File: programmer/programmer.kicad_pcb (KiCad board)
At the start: 2 copper layers, 63 x 30 mm, 54 parts, among them J1 USB_C_Receptacle_USB2.0_14P, U1 FT2232HL, U2 74LVC2T45DC, U3 93CxxA, U4 NLSV2T244DM, U5 NLSV2T244DM, U6 NLSV2T244DM, U8 AMS1117-3.3, Y1 12MHz

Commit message: Programmer bring-up changes and notes
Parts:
- added C20: 3.3u, Capacitor_SMD:C_0603_1608Metric_Pad1.08x0.95mm_HandSolder, F.Cu at (59.6, 35.5)
- added C21: 3.3u, Capacitor_SMD:C_0603_1608Metric_Pad1.08x0.95mm_HandSolder, F.Cu at (59.9, 30.4)
- added C22: 3.3u, Capacitor_SMD:C_0603_1608Metric_Pad1.08x0.95mm_HandSolder, F.Cu at (59.8, 25.3)
- added R12: 2.2, Resistor_SMD:R_0603_1608Metric_Pad0.98x0.95mm_HandSolder, F.Cu at (83.6, 22.4)
- added TP1: TestPoint, TestPoint:TestPoint_THTPad_1.0x1.0mm_Drill0.5mm, F.Cu at (72.5, 23.6)
- added TP2: TestPoint, TestPoint:TestPoint_THTPad_1.0x1.0mm_Drill0.5mm, F.Cu at (70.4, 23.6)
- added TP3: TestPoint, TestPoint:TestPoint_THTPad_1.0x1.0mm_Drill0.5mm, F.Cu at (70.4, 25.7)
- added TP4: TestPoint, TestPoint:TestPoint_THTPad_1.0x1.0mm_Drill0.5mm, F.Cu at (69.6, 37.0)
- added TP5: TestPoint, TestPoint:TestPoint_THTPad_1.0x1.0mm_Drill0.5mm, F.Cu at (69.6, 34.9)
- added TP6: TestPoint, TestPoint:TestPoint_THTPad_1.0x1.0mm_Drill0.5mm, F.Cu at (69.6, 32.8)
- C6: value 3.3u -> 22u; footprint Capacitor_SMD:C_0603_1608Metric_Pad1.08x0.95mm_HandSolder -> Capacitor_SMD:C_0805_2012Metric_Pad1.18x1.45mm_HandSolder
- moved C7 0.70 mm to (85.9, 26.9), turned to -90 degrees
- moved C6 0.12 mm to (85.5, 22.6), turned to 90 degrees
- turned D4 to 90 degrees
- turned D5 to 90 degrees
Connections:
- C6 pad 2: GND -> Net-(C6-Pad2)
- D4 pad 1: VCC -> Net-(D4-K)
- D4 pad 2: Net-(D4-A) -> VCC
- D5 pad 1: VIO -> Net-(D5-K)
- D5 pad 2: Net-(D5-A) -> VIO
- R10 pad 1: Net-(D4-A) -> Net-(D4-K)
- R11 pad 1: Net-(D5-A) -> Net-(D5-K)
- U1 pad 32: unconnected-(U1-ACBUS5-Pad32) -> Net-(U1-ACBUS5)
- U1 pad 33: unconnected-(U1-ACBUS6-Pad33) -> Net-(U1-ACBUS6)
- U1 pad 34: unconnected-(U1-ACBUS7-Pad34) -> Net-(U1-ACBUS7)
- U1 pad 45: unconnected-(U1-BDBUS6-Pad45) -> Net-(U1-BDBUS6)
- U1 pad 46: unconnected-(U1-BDBUS7-Pad46) -> Net-(U1-BDBUS7)
- U1 pad 48: unconnected-(U1-BCBUS0-Pad48) -> Net-(U1-BCBUS0)
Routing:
- net Net-(U1-ACBUS6): track 0.00 -> 4.62 mm
- net Net-(U1-BCBUS0): track 0.00 -> 3.53 mm
- net Net-(U1-ACBUS7): track 0.00 -> 3.48 mm
- net GND: track 52.3 -> 55.7 mm, vias 44 -> 46
- net Net-(U1-ACBUS5): track 0.00 -> 2.92 mm
- net Net-(U1-BDBUS7): track 0.00 -> 2.78 mm
- net Net-(U1-BDBUS6): track 0.00 -> 2.74 mm
- net Net-(C6-Pad2): track 0.00 -> 1.98 mm
- net Net-(D5-K): track 0.00 -> 1.71 mm
- net Net-(D5-A): track 1.71 -> 0.00 mm
- net Net-(D4-K): track 0.00 -> 1.71 mm
- net Net-(D4-A): track 1.71 -> 0.00 mm
- net Net-(JP4-A): track 7.23 -> 8.60 mm
- net /FT_JTAG_SEL_N: track 24.1 -> 25.1 mm
- net /FT_JTAG_TMS: track 25.2 -> 26.2 mm
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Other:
- board text added: "J_SEL"
- board text added: "RCFG"
- board text added: "RXD"
- board text added: "TXD"
- board text removed: "JTAG_SEL"
- board text removed: "RECONFIG"
- board text removed: "SER_RXD"
- board text removed: "SER_TXD"

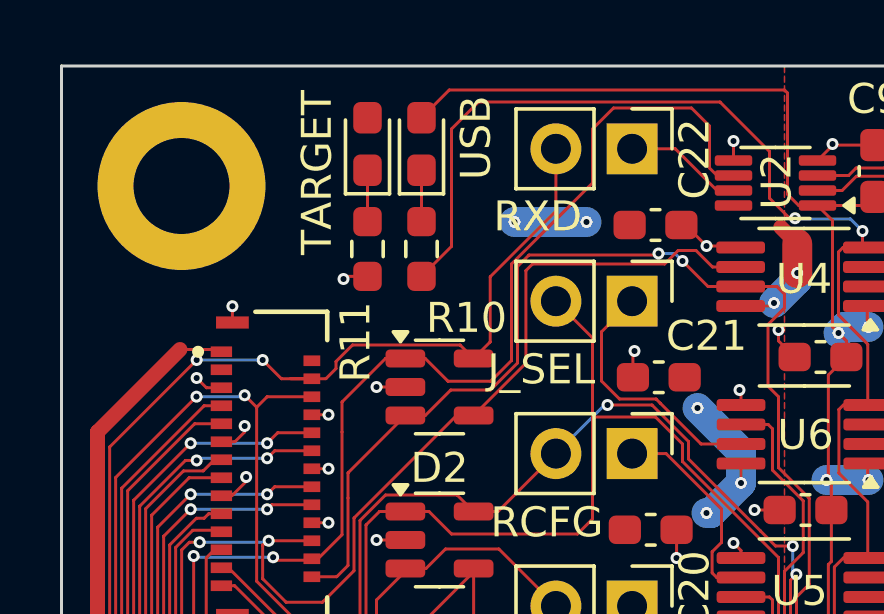
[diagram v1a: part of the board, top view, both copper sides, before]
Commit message: Updated programmer schematic and PCBs.
All known changes are incorporated.

p.s.: I decided to stick with this rather sketchy LDO.
The reason for this is that it's heatsink tab is connected
to VCC, which happens to be the fill on the top layer
so a GND-connected alternative would be less well cooled.
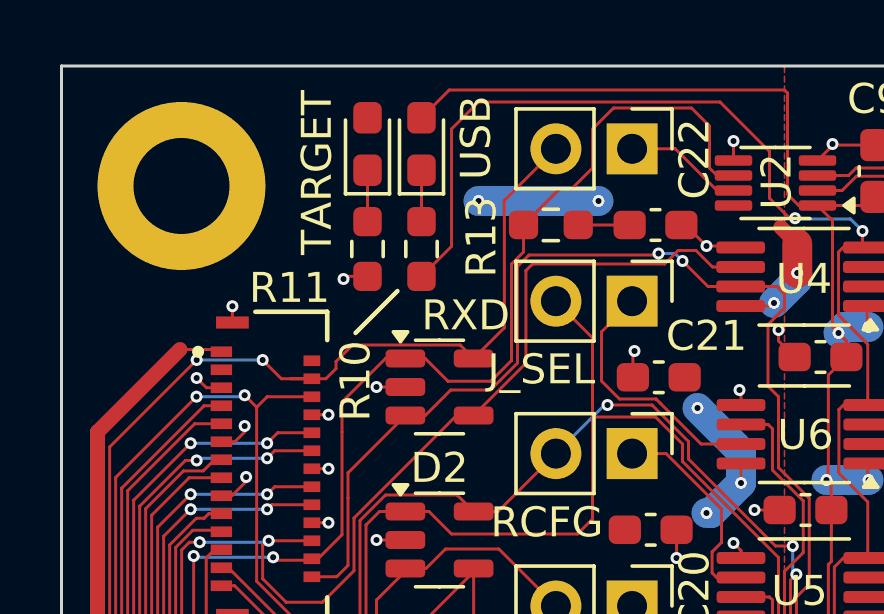
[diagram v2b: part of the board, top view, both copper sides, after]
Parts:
- added R13: 10k, Resistor_SMD:R_0603_1608Metric_Pad0.98x0.95mm_HandSolder, F.Cu at (56.3, 25.3)
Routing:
- net VIO: track 12.4 -> 15.7 mm
